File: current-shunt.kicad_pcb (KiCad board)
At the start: 4 copper layers, 130 x 50 mm, 183 parts, among them J1 Screw_Terminal_01x03, J2 Screw_Terminal_01x03, J3 Screw_Terminal_01x03, J4 Conn_01x02, J5 Conn_01x04, J6 Conn_01x04, U1 ADS1015IDGS, U2 INA219AxD, U3 INA219AxD, U4 INA219AxD, U5 MCP9804_MSOP, U6 M24C02-WMN, U7 TSR_1-2450, U8 ISO1541, U9 SRV05-4

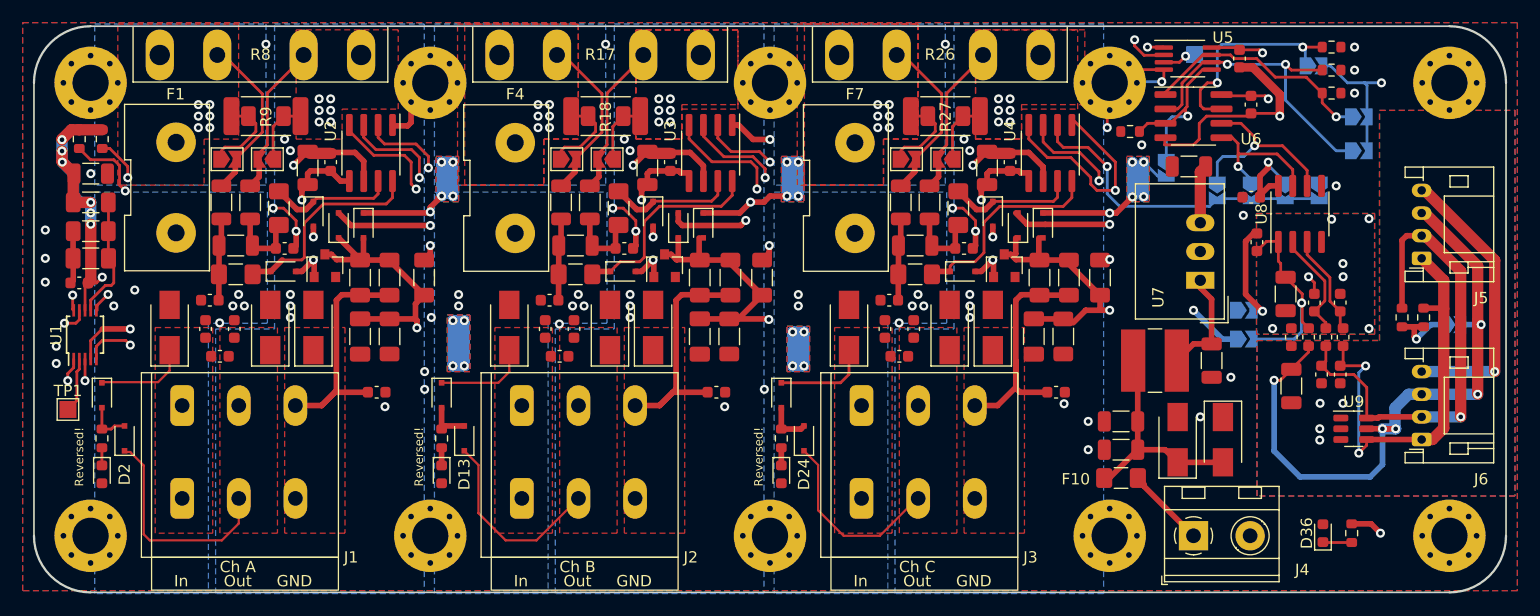
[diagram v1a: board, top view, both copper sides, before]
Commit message: Add JLCPCB rotation offsets
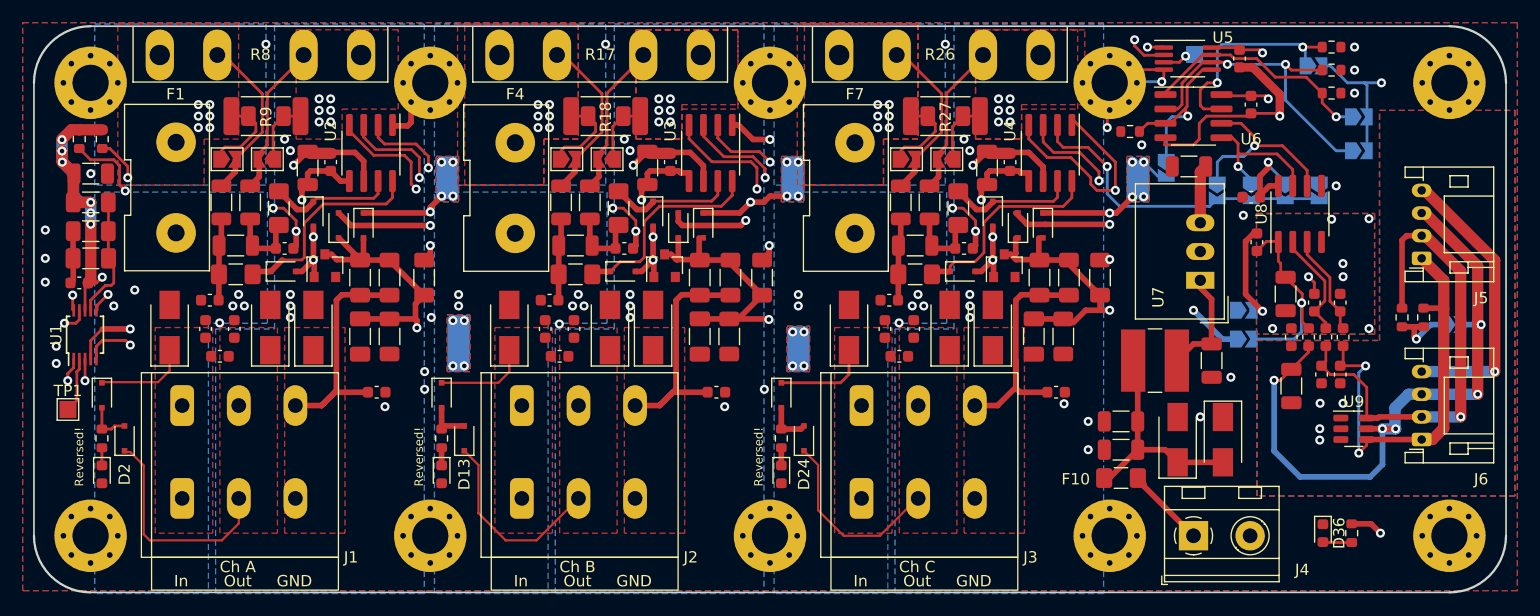
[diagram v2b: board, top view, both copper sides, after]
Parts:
- turned D36 to -90 degrees
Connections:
- D36 pad 1: Net-(D36-Pad1) -> GND
- D36 pad 2: GND -> Net-(D36-Pad2)
- R36 pad 2: Net-(D36-Pad1) -> Net-(D36-Pad2)
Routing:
- net Net-(D36-Pad2): track 0.00 -> 2.56 mm
- net Net-(D36-Pad1): track 2.56 -> 0.00 mm
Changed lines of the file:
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@@
   (net 57 "Net-(D28-Pad1)")
   (net 58 "Net-(D29-Pad1)")
-  (net 59 "Net-(D36-Pad1)")
+  (net 59 "Net-(D36-Pad2)")
   (net 60 "Net-(F10-Pad1)")
   (net 61 "Net-(JP1-Pad2)")
@@
     (descr "SOIC, 8 Pin (JEDEC MS-012AA, https://www.analog.com/media/en/package-pcb-resources/package/pkg_pdf/soic_narrow-r/r_8.pdf), generated with kicad-footprint-generator ipc_gullwing_generator.py")
     (tags "SOIC SO")
+    (property "JLCPCB Rotation Offset" "-90")
     (property "LCSC Part #" "C138706")
     (property "Sheetfile" "File: shunt.kicad_sch")
@@
   )
   (footprint "LED_SMD:LED_0603_1608Metric" (layer "F.Cu")
-    (at 163.83 64.77 90)
+    (at 163.83 64.77 -90)
     (descr "LED SMD 0603 (1608 Metric), square (rectangular) end terminal, IPC_7351 nominal, (Body size source: http://www.tortai-tech.com/upload/download/2011102023233369053.pdf), generated with kicad-footprint-generator")
     (tags "LED")
@@
     (fp_line (start 0.8 -0.4) (end -0.5 -0.4) (layer "F.Fab") (width 0.1))
     (fp_line (start -0.5 -0.4) (end -0.8 -0.1) (layer "F.Fab") (width 0.1))
-    (pad "1" smd roundrect (at -0.7875 0 90) (size 0.875 0.95) (layers "F.Cu" "F.Paste" "F.Mask") (roundrect_rratio 0.25)
-      (net 59 "Net-(D36-Pad1)") (pinfunction "K") (pintype "passive"))
-    (pad "2" smd roundrect (at 0.7875 0 90) (size 0.875 0.95) (layers "F.Cu" "F.Paste" "F.Mask") (roundrect_rratio 0.25)
-      (net 2 "GND") (pinfunction "A") (pintype "passive"))
+    (pad "1" smd roundrect (at -0.7875 0 270) (size 0.875 0.95) (layers "F.Cu" "F.Paste" "F.Mask") (roundrect_rratio 0.25)
+      (net 2 "GND") (pinfunction "K") (pintype "passive"))
+    (pad "2" smd roundrect (at 0.7875 0 270) (size 0.875 0.95) (layers "F.Cu" "F.Paste" "F.Mask") (roundrect_rratio 0.25)
+      (net 59 "Net-(D36-Pad2)") (pinfunction "A") (pintype "passive"))
     (model "${KICAD6_3DMODEL_DIR}/LED_SMD.3dshapes/LED_0603_1608Metric.wrl"
       (offset (xyz 0 0 0))
@@
     (descr "SOT-23, Single Diode")
     (tags "SOT-23")
+    (property "JLCPCB Rotation Offset" "180")
     (property "LCSC Part #" "C118567")
     (property "Sheetfile" "File: shunt.kicad_sch")
@@
     (descr "SOT-23, Single Diode")
     (tags "SOT-23")
+    (property "JLCPCB Rotation Offset" "180")
     (property "LCSC Part #" "C118567")
     (property "Sheetfile" "File: shunt.kicad_sch")
@@
     (descr "SOIC, 8 Pin (JEDEC MS-012AA, https://www.analog.com/media/en/package-pcb-resources/package/pkg_pdf/soic_narrow-r/r_8.pdf), generated with kicad-footprint-generator ipc_gullwing_generator.py")
     (tags "SOIC SO")
+    (property "JLCPCB Rotation Offset" "-90")
     (property "LCSC Part #" "C138706")
     (property "Sheetfile" "File: shunt.kicad_sch")
@@
     (descr "SOIC, 8 Pin (JEDEC MS-012AA, https://www.analog.com/media/en/package-pcb-resources/package/pkg_pdf/soic_narrow-r/r_8.pdf), generated with kicad-footprint-generator ipc_gullwing_generator.py")
     (tags "SOIC SO")
+    (property "JLCPCB Rotation Offset" "-90")
     (property "LCSC Part #" "C138706")
     (property "Sheetfile" "File: shunt.kicad_sch")
@@
       (net 4 "+5V") (pintype "passive"))
     (pad "2" smd roundrect (at 0.825 0 270) (size 0.8 0.95) (layers "F.Cu" "F.Paste" "F.Mask") (roundrect_rratio 0.25)
-      (net 59 "Net-(D36-Pad1)") (pintype "passive"))
+      (net 59 "Net-(D36-Pad2)") (pintype "passive"))
     (model "${KICAD6_3DMODEL_DIR}/Resistor_SMD.3dshapes/R_0603_1608Metric.wrl"
       (offset (xyz 0 0 0))
@@
     (descr "SOIC, 8 Pin (JEDEC MS-012AA, https://www.analog.com/media/en/package-pcb-resources/package/pkg_pdf/soic_narrow-r/r_8.pdf), generated with kicad-footprint-generator ipc_gullwing_generator.py")
     (tags "SOIC SO")
+    (property "JLCPCB Rotation Offset" "-90")
     (property "LCSC Part #" "C143028")
     (property "Sheetfile" "File: i2c.kicad_sch")
@@
     (descr "TSSOP10: plastic thin shrink small outline package; 10 leads; body width 3 mm; (see NXP SSOP-TSSOP-VSO-REFLOW.pdf and sot552-1_po.pdf)")
     (tags "SSOP 0.5")
+    (property "JLCPCB Rotation Offset" "-90")
     (property "LCSC Part #" "C193969")
     (property "Sheetfile" "File: gnd-level.kicad_sch")
@@
     (descr "SOT, 6 Pin (https://www.jedec.org/sites/default/files/docs/Mo-178c.PDF variant AB), generated with kicad-footprint-generator ipc_gullwing_generator.py")
     (tags "SOT TO_SOT_SMD")
+    (property "JLCPCB Rotation Offset" "180")
     (property "LCSC Part #" "C85364")
     (property "Sheetfile" "File: i2c.kicad_sch")
@@
     (descr "SOT-23, Single Diode")
     (tags "SOT-23")
+    (property "JLCPCB Rotation Offset" "180")
     (property "LCSC Part #" "C118567")
     (property "Sheetfile" "File: shunt.kicad_sch")
@@
     (descr "SOIC, 8 Pin (JEDEC MS-012AA, https://www.analog.com/media/en/package-pcb-resources/package/pkg_pdf/soic_narrow-r/r_8.pdf), generated with kicad-footprint-generator ipc_gullwing_generator.py")
     (tags "SOIC SO")
+    (property "JLCPCB Rotation Offset" "-90")
     (property "LCSC Part #" "C7562")
     (property "Sheetfile" "File: temp-eeprom.kicad_sch")
@@
   (segment (start 134.676 38.608) (end 134.676 37.676) (width 0.5) (layer "F.Cu") (net 2))
   (segment (start 132.9225 32.2825) (end 134.168 31.037) (width 0.5) (layer "F.Cu") (net 2))
+  (segment (start 104.676 38.608) (end 104.676 40.64) (width 0.5) (layer "F.Cu") (net 2))
   (segment (start 73.152 39.383) (end 72.911 39.624) (width 0.5) (layer "F.Cu") (net 2))
   (segment (start 73.152 38.1) (end 73.152 39.383) (width 0.5) (layer "F.Cu") (net 2))
@@
   (segment (start 136.7 36.492) (end 137.708 37.5) (width 0.5) (layer "F.Cu") (net 2))
   (segment (start 76.2 31.229) (end 76.28152 31.14748) (width 0.25) (layer "F.Cu") (net 2))
+  (segment (start 134.676 38.608) (end 134.676 40.64) (width 0.5) (layer "F.Cu") (net 2))
   (segment (start 134.36 31.229) (end 134.168 31.037) (width 0.25) (layer "F.Cu") (net 2))
   (segment (start 139.121 32.421) (end 139.121 32.955) (width 0.5) (layer "F.Cu") (net 2))
@@
   (segment (start 106.2 31.229) (end 104.36 31.229) (width 1) (layer "F.Cu") (net 2))
   (segment (start 74.676 38.608) (end 74.676 37.676) (width 0.5) (layer "F.Cu") (net 2))
-  (segment (start 104.742 40.706) (end 104.676 40.64) (width 0.25) (layer "F.Cu") (net 2))
   (segment (start 73.152 37.179507) (end 73.152 38.1) (width 0.25) (layer "F.Cu") (net 2))
   (segment (start 76.9 36.492) (end 78.008 37.6) (width 0.5) (layer "F.Cu") (net 2))
@@
   (segment (start 157.48 27.699) (end 159.779 27.699) (width 0.25) (layer "F.Cu") (net 2))
   (segment (start 76.28152 31.14748) (end 78.34748 31.14748) (width 0.5) (layer "F.Cu") (net 2))
+  (segment (start 104.676 40.64) (end 104.742 40.706) (width 0.5) (layer "F.Cu") (net 2))
   (segment (start 147.5 23.5) (end 146.5 23.5) (width 0.25) (layer "F.Cu") (net 2))
   (segment (start 74.742 42.148) (end 74.742 40.706) (width 0.5) (layer "F.Cu") (net 2))
   (segment (start 157.635 23.635) (end 156.464 23.635) (width 0.75) (layer "F.Cu") (net 2))
   (segment (start 103.152 37.179507) (end 103.152 38.1) (width 0.25) (layer "F.Cu") (net 2))
+  (segment (start 74.676 38.608) (end 74.676 40.64) (width 0.5) (layer "F.Cu") (net 2))
   (segment locked (start 54.508 49.394) (end 54.508 51.308) (width 0.25) (layer "F.Cu") (net 2))
   (segment (start 103.152 39.383) (end 102.911 39.624) (width 0.5) (layer "F.Cu") (net 2))
@@
   (via (at 74.676 38.608) (size 0.8) (drill 0.4) (layers "F.Cu" "B.Cu") (free) (net 2))
   (via (at 156.8 36.7) (size 0.8) (drill 0.4) (layers "F.Cu" "B.Cu") (free) (net 2))
-  (segment (start 134.676 40.64) (end 134.676 38.608) (width 1) (layer "In1.Cu") (net 2))
-  (segment (start 74.676 40.64) (end 74.676 38.608) (width 1) (layer "In1.Cu") (net 2))
   (segment (start 73.66 38.608) (end 73.152 38.1) (width 1) (layer "In1.Cu") (net 2))
   (segment (start 104.676 38.608) (end 103.66 38.608) (width 1) (layer "In1.Cu") (net 2))
   (segment (start 134.676 38.608) (end 133.66 38.608) (width 1) (layer "In1.Cu") (net 2))
   (segment (start 74.676 38.608) (end 73.66 38.608) (width 1) (layer "In1.Cu") (net 2))
-  (segment (start 104.676 40.64) (end 104.676 38.608) (width 1) (layer "In1.Cu") (net 2))
   (segment (start 103.66 38.608) (end 103.152 38.1) (width 1) (layer "In1.Cu") (net 2))
   (segment (start 133.66 38.608) (end 133.152 38.1) (width 1) (layer "In1.Cu") (net 2))

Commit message: Add JLCPCB tooling and marking
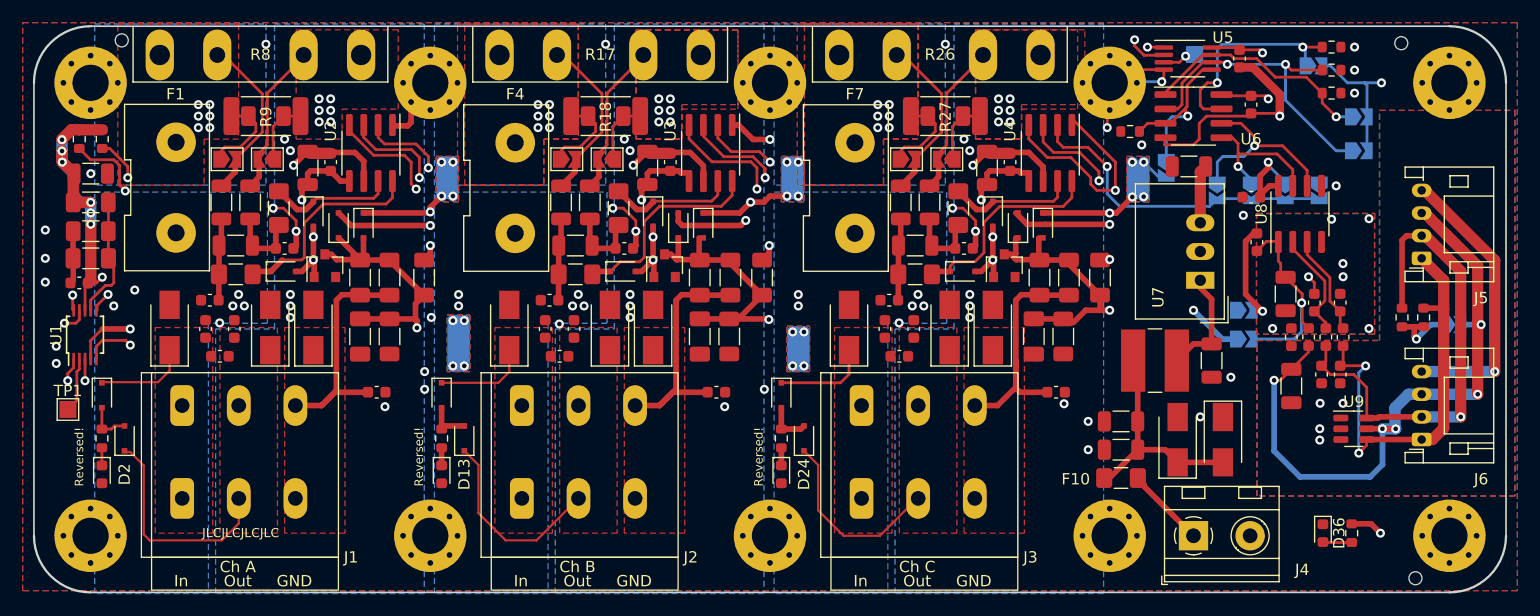
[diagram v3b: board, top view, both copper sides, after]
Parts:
- added REF**: JLCPCB_Order_No, Project_Footprints:JLCPCB_Order_No, F.Cu at (68.2, 64.8)
- added REF**: JLCPCB_SMT_Tooling_Hole, Project_Footprints:JLCPCB_SMT_Tooling_Hole, F.Cu at (57.8, 21.2)
- added REF**: JLCPCB_SMT_Tooling_Hole, Project_Footprints:JLCPCB_SMT_Tooling_Hole, F.Cu at (170.8, 21.5)
- added REF**: JLCPCB_SMT_Tooling_Hole, Project_Footprints:JLCPCB_SMT_Tooling_Hole, F.Cu at (172.0, 68.8)
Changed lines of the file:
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@@
     )
   )
+  (footprint "Project_Footprints:JLCPCB_Order_No" (layer "F.Cu")
+    (at 68.25 64.75)
+    (attr board_only exclude_from_pos_files exclude_from_bom)
+    (fp_text reference "REF**" (at 0 -0.5 unlocked) (layer "F.SilkS") hide
+      (effects (font (size 1 1) (thickness 0.15)))
+    )
+    (fp_text value "JLCPCB_Order_No" (at 0 1 unlocked) (layer "F.Fab") hide
+      (effects (font (size 1 1) (thickness 0.15)))
+    )
+    (fp_text user "JLCJLCJLCJLC" (at 0 0 unlocked) (layer "F.SilkS")
+      (effects (font (size 0.8 0.8) (thickness 0.15)))
+    )
+    (fp_text user "${REFERENCE}" (at 0 2.5 unlocked) (layer "F.Fab") hide
+      (effects (font (size 1 1) (thickness 0.15)))
+    )
+  )
   (footprint "Project_Footprints:Wago_2604-1103" (layer "F.Cu")
     (at 63.085502 53.5)
@@
     )
   )
+  (footprint "Project_Footprints:JLCPCB_SMT_Tooling_Hole" (layer "F.Cu")
+    (at 57.75 21.25)
+    (attr board_only exclude_from_bom)
+    (fp_text reference "REF**" (at 0 -0.5 unlocked) (layer "F.SilkS") hide
+      (effects (font (size 1 1) (thickness 0.15)))
+    )
+    (fp_text value "JLCPCB_SMT_Tooling_Hole" (at 0 1 unlocked) (layer "F.Fab") hide
+      (effects (font (size 1 1) (thickness 0.15)))
+    )
+    (fp_text user "${REFERENCE}" (at 0 2.5 unlocked) (layer "F.Fab") hide
+      (effects (font (size 1 1) (thickness 0.15)))
+    )
+    (pad "" np_thru_hole circle (at 0 0) (size 1.3 1.3) (drill 1.152) (layers *.Mask))
+  )
   (footprint "Diode_SMD:D_SOD-323F" (layer "F.Cu")
     (at 56 52.59 -90)
@@
       (net 2 "GND") (pinfunction "1") (pintype "input"))
   )
+  (footprint "Project_Footprints:JLCPCB_SMT_Tooling_Hole" (layer "F.Cu")
+    (at 170.75 21.5)
+    (attr board_only exclude_from_bom)
+    (fp_text reference "REF**" (at 0 -0.5 unlocked) (layer "F.SilkS") hide
+      (effects (font (size 1 1) (thickness 0.15)))
+    )
+    (fp_text value "JLCPCB_SMT_Tooling_Hole" (at 0 1 unlocked) (layer "F.Fab") hide
+      (effects (font (size 1 1) (thickness 0.15)))
+    )
+    (fp_text user "${REFERENCE}" (at 0 2.5 unlocked) (layer "F.Fab") hide
+      (effects (font (size 1 1) (thickness 0.15)))
+    )
+    (pad "" np_thru_hole circle (at 0 0) (size 1.3 1.3) (drill 1.152) (layers *.Mask))
+  )
   (footprint "Package_SO:SOIC-8_3.9x4.9mm_P1.27mm" (layer "F.Cu")
     (at 152.4 27.94)
@@
     )
   )
+  (footprint "Project_Footprints:JLCPCB_SMT_Tooling_Hole" (layer "F.Cu")
+    (at 172 68.75)
+    (attr board_only exclude_from_bom)
+    (fp_text reference "REF**" (at 0 -0.5 unlocked) (layer "F.SilkS") hide
+      (effects (font (size 1 1) (thickness 0.15)))
+    )
+    (fp_text value "JLCPCB_SMT_Tooling_Hole" (at 0 1 unlocked) (layer "F.Fab") hide
+      (effects (font (size 1 1) (thickness 0.15)))
+    )
+    (fp_text user "${REFERENCE}" (at 0 2.5 unlocked) (layer "F.Fab") hide
+      (effects (font (size 1 1) (thickness 0.15)))
+    )
+    (pad "" np_thru_hole circle (at 0 0) (size 1.3 1.3) (drill 1.152) (layers *.Mask))
+  )
   (footprint "Project_Footprints:R_Shunt_Isabellenhuette_PBV" (layer "F.Cu")
     (at 100 19.98)
@@
     (effects (font (size 1.5 1.5) (thickness 0.25)) (justify left mirror))
   )
-  (gr_text "EEPROM\nWP" (at 165 23) (layer "B.SilkS")
+  (gr_text "EEPROM\nWP" (at 165 23.75) (layer "B.SilkS")
     (effects (font (size 1 1) (thickness 0.15)) (justify right mirror))
   )
